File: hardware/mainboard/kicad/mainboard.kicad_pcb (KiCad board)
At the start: 4 copper layers, 54 x 120 mm, 134 parts, among them J1 XT30PW-M, J10 J_PYRO2, J11 J_GPS, J12 J_QWIIC, J13 J_CAM, J14 J_LED, J15 J_EXP, J2 J_BAT1, J3 J_SW, J4 J_ARM, J5 J_SERVO1, J6 J_SERVO2, J7 J_SERVO3, J8 J_MOT, J9 J_PYRO1, Q1 AO3401A, Q2 AO3401A, Q3 AO3400A, Q4 AO3400A, Q5 AO3400A, U1 TPS563201DDCR, U10 E22-400T22S, U2 TPS63070RNMR, U3 AP2112K-3.3TRG1, U4 ICM-42688-P, U5 BMP390, U6 INA219AIDR, U7 DRV8833PWPR, U8 74AHCT1G125, U9 74AHCT1G125

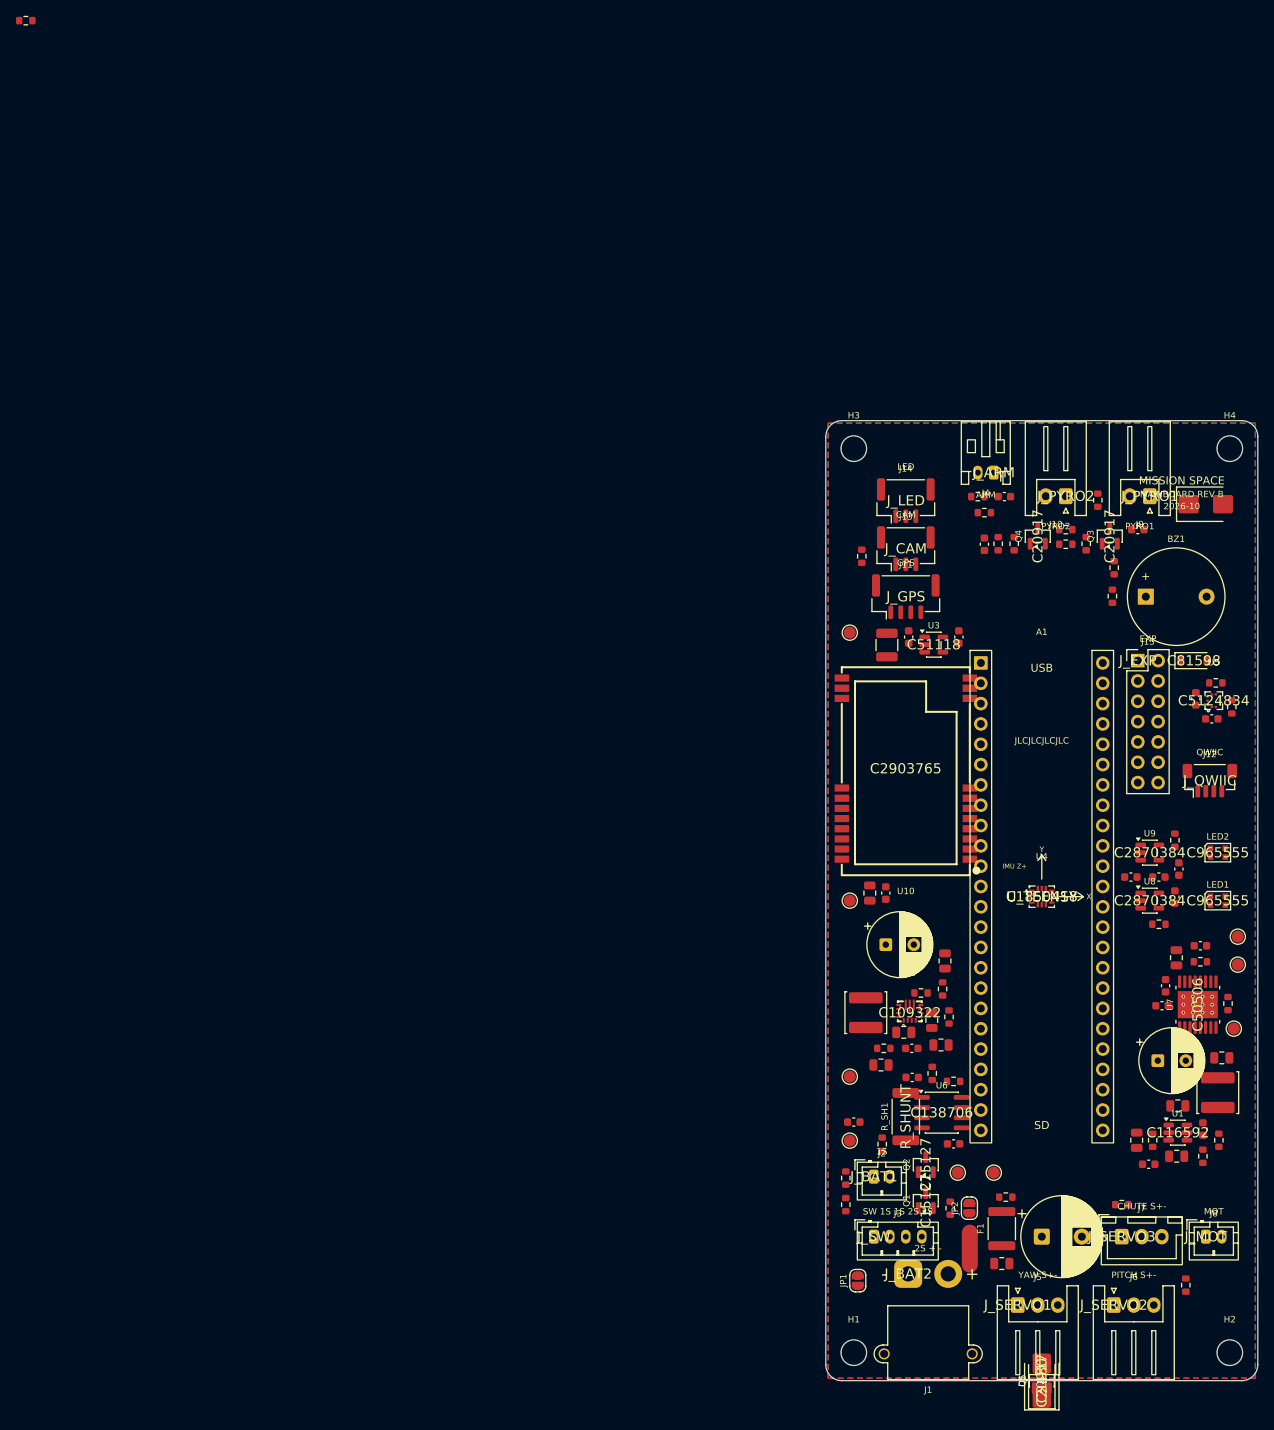
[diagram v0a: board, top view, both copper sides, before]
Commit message: Platine rev B geroutet: alle 134 Footprints platziert, DRC ohne Fehler, 3 offene Verbindungen; Renders und Lagenbilder; Fertigervergleich
- Lagen: In1 GND, B.Cu geteilte Versorgungsflaeche GND_PWR/5V_SYS, Plane-Vias an jedem SMD-Pad
- Freerouting 2.5.0 (JAR, Temurin 25) mit zwei Nachlaeufen auf fixierter Verdrahtung und kollisionsgeprueften Stummeln
- check_design.py: Netzliste gegen Spezifikation §4 (OK), make.sh fuer die ganze Kette
- 3D-Modelle Teensy 4.1 und XT30PW-M (CadQuery), Renders und layers.pdf in kicad/img
- Fertiger_2026-10-21.md: JLCPCB empfohlen, Aisler als EU-Rueckfall, BMP390 bei JLC nicht lieferbar
- naechster Schritt laut kicad/README.md §8: Review-Punkte A1-A5 (review_kicad_2026-10-21.md) vor dem Handrouting

Co-Authored-By: Claude Opus 5.5 <noreply@anthropic.com>
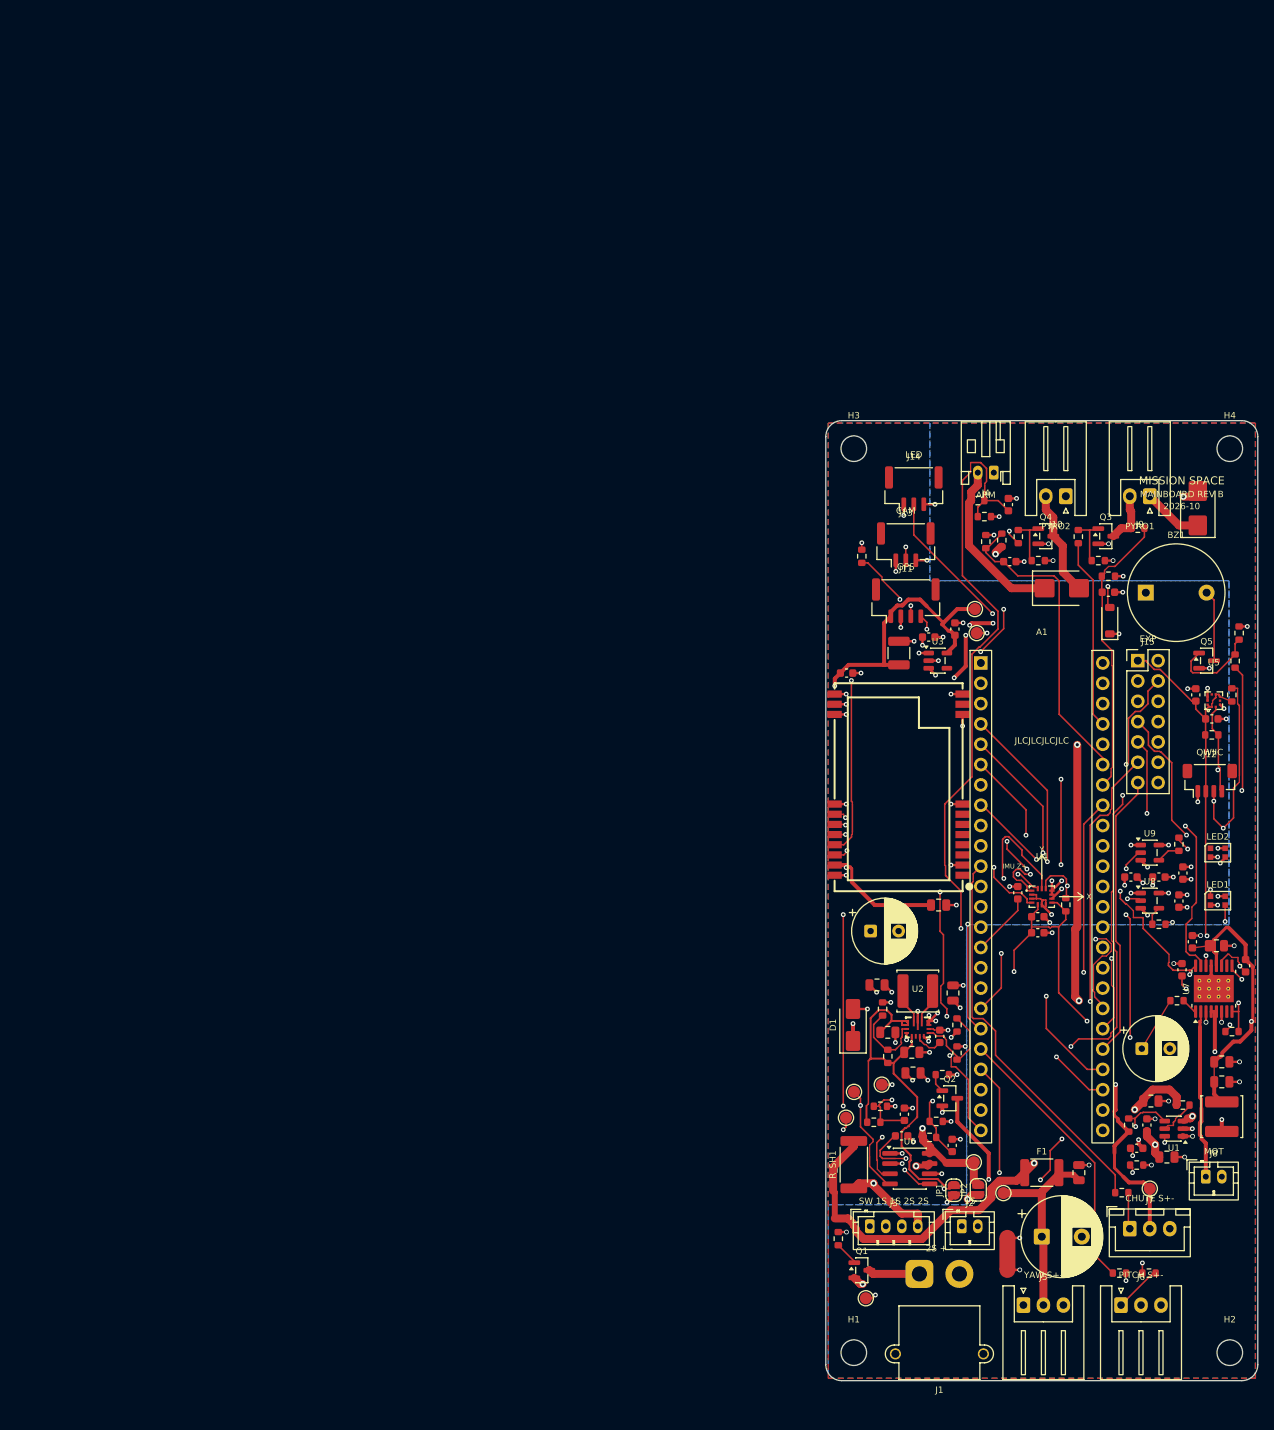
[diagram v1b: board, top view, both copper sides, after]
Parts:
- moved R35 169.9 mm to (151.7, 76.5), turned to 90 degrees
- moved D3 99.1 mm to (129.5, 70.9), turned to 0 degrees
- moved R34 93.1 mm to (151.2, 80.0)
- moved Q5 92.3 mm to (147.6, 80.0), turned to 0 degrees
- moved C24 61.1 mm to (124.0, 109.0)
- moved R14 59.6 mm to (130.0, 110.5)
- moved C23 58.0 mm to (126.5, 112.0), turned to 0 degrees
- moved C25 56.0 mm to (126.5, 114.0), turned to 0 degrees
- moved TP8 52.6 mm to (102.5, 137.1)
- moved TP9 51.8 mm to (103.5, 133.9)
- moved D1 50.3 mm to (103.4, 125.5)
- moved TP3 37.0 mm to (118.9, 76.5)
- moved C29 27.9 mm to (102.6, 81.5), turned to 0 degrees
- moved TP2 27.8 mm to (105.0, 159.7)
- moved TP5 22.6 mm to (140.5, 146.0)
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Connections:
- LED2 pad 1: (no net) -> unconnected-(LED2-DOUT-Pad1)
- U10 pad 1: (no net) -> unconnected-(U10-RESET-Pad1)
- U10 pad 12: (no net) -> unconnected-(U10-ANT-Pad12)
- U10 pad 3: (no net) -> unconnected-(U10-NC-Pad3)
- U10 pad 4: (no net) -> unconnected-(U10-NC-Pad4)
- U10 pad 5: (no net) -> unconnected-(U10-NC-Pad5)
- U10 pad 6: (no net) -> unconnected-(U10-NC-Pad6)
- U10 pad 7: (no net) -> unconnected-(U10-NC-Pad7)
- U2 pad 2: (no net) -> unconnected-(U2-PG-Pad2)
- U3 pad 4: (no net) -> unconnected-(U3-NC-Pad4)
- U5 pad 7: (no net) -> unconnected-(U5-INT-Pad7)
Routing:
- net LORA_M0: track 0.00 -> 176.7 mm, vias 0 -> 1
- net 3V3: track 0.00 -> 176.6 mm, vias 0 -> 6
- net SDA: track 0.00 -> 162.6 mm, vias 0 -> 8
- net LORA_TXD: track 0.00 -> 150.1 mm, vias 0 -> 3
- net VBAT_PROT: track 0.00 -> 138.4 mm, vias 0 -> 4
- net LORA_AUX: track 0.00 -> 109.7 mm, vias 0 -> 2
- net VBAT_MEAS: track 0.00 -> 107.8 mm, vias 0 -> 5
- net 5V_SERVO: track 0.00 -> 104.6 mm, vias 0 -> 2
- net SCL: track 0.00 -> 100.7 mm, vias 0 -> 3
- net GND: track 0.00 -> 90.9 mm, vias 0 -> 70
- net LORA_M1: track 0.00 -> 88.6 mm, vias 0 -> 4
- net ARM_SENSE: track 0.00 -> 84.5 mm, vias 0 -> 1
- net TEENSY_VIN: track 0.00 -> 80.3 mm, vias 0 -> 5
- net LED_EXT_DATA: track 0.00 -> 77.2 mm, vias 0 -> 2
- net VSYS_IN: track 0.00 -> 76.6 mm, vias 0 -> 2
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- added copper zone on B.Cu, net 5V_SYS
- added copper zone on B.Cu, net GND_PWR
- removed copper zone on B.Cu, net GND

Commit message: Kartonaut: Name, Missionsabzeichen, Bestückungsdruck neu, Lötstopp blau
- Projekt heißt Kartonaut (Karton + Astronaut); Flüge werden hochgezählt, Erstflug = Kartonaut 1
- Abzeichen als Polygone in hardware/mainboard/kicad/logo.py, SVGs in docs/brand/
- spacecode/ -> firmware/, Bodenstation-Repo groundcode -> kartonaut-ground (Links, .gitignore)
- gen_pcb.py silk: Bestückungsdruck nur neu setzen, auf der gerouteten Platine; 1,0 mm Schrift,
  freie Plätze statt Überlappungen, Kurznamen an den Steckern, Testpunkte mit Netznamen,
  kleines Abzeichen vorn; hinten Abzeichen 20 mm und Steckerbelegung
- Stackup JLC04161H-7628 mit blauem Lötstopp im Board, Renders mit Stackup-Farben
- DRC-Druckwarnungen 167 -> 14 (Rest aus Footprint-Umrissen)

Co-Authored-By: Claude Opus 5.5 <noreply@anthropic.com>
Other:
- board text added: "+ -"
- board text added: "1:3V3 2:GND 14:5V"
- board text added: "1S 1S 2S 2S"
- board text added: "2S"
- board text added: "2S ARM"
- board text added: "3V3 GND TX RX"
- board text added: "3V3RF"
- board text added: "5V"
- board text added: "5V DAT GND"
- board text added: "5V TRG GND"
- board text added: "5VS"
- board text added: "A B"
- board text added: "CHUTE"
- board text added: "GND"
- board text added: "GND 3V3 SDA SCL"
- board text added: "J1 2S"
- board text added: "J10 PYRO2"
- board text added: "J11 GPS"
- board text added: "J12 QWIIC"
- board text added: "J13 CAM"
- board text added: "J14 LED"
- board text added: "J15 EXP"
- board text added: "J2 1S"
- board text added: "J3 SW"
- board text added: "J4 ARM"
- board text added: "J5 YAW"
- board text added: "J6 PITCH"
- board text added: "J7 CHUTE"
- board text added: "J8 MOT"
- board text added: "J9 PYRO1"
- board text added: "PIN 1 ZUERST"
- board text added: "PITCH"
- board text added: "S + -"
- board text added: "S 5V -"
- board text added: "STECKER"
- board text added: "SW"
- board text added: "VSYS"
- board text added: "YAW"
- board text removed: "2S + -"
- board text removed: "CHUTE S+-"
- board text removed: "MAINBOARD REV B"
- board text removed: "MISSION SPACE"
- board text removed: "PITCH S+-"
- board text removed: "PYRO2"
- board text removed: "SW 1S 1S 2S 2S"
- board text removed: "YAW S+-"
